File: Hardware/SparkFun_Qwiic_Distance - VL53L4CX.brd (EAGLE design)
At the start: 25.4 x 25.4 mm, 25 parts, among them J2 QWIIC_RIGHT_ANGLE, J4 QWIIC_RIGHT_ANGLE, U1 VL53L4X

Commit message: Adds silk to the product
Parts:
- added LOGO2: SFE_LOGO_NAME.1_INCH, SparkFun-Aesthetics:SFE_LOGO_NAME_.1
- added LOGO3: QWIIC_LOGO_4MM, SparkFun-Aesthetics:QWIIC_4MM
- added U$1: (no value), distanceSensor:##INT##7
- added U$10: (no value), distanceSensor:#LED#54
- added U$11: (no value), distanceSensor:#INT#55
- added U$12: (no value), distanceBot:##INT##7
- added U$13: (no value), distanceBot:##SHUT##6
- added U$14: (no value), distanceBot:#3V3#1
- added U$15: (no value), distanceBot:#GND#0
- added U$16: (no value), distanceBot:#SCL#4
- added U$17: (no value), distanceBot:#SDA#5
- added U$18, U$8: (no value), distanceSensor:DISTANCE_SENSOR8
- added U$19, U$9: (no value), distanceSensor:VL53L4CX9
- added U$2: (no value), distanceSensor:##SHUT##6
- added U$20: (no value), distanceSensor:DEF_ADDR#54
- added U$21: (no value), distanceSensor:0X2955
- added U$22: (no value), SparkFun-Aesthetics:SFE_LOGO_FLAME_.1
- added U$3: (no value), distanceSensor:#3V3#1
- added U$4: (no value), distanceSensor:#GND#0
- added U$5: (no value), distanceSensor:#I2C#56
- added U$6: (no value), distanceSensor:#SCL#4
- added U$7: (no value), distanceSensor:#SDA#5
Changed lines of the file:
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@@
 <layer number="45" name="Holes" color="7" fill="1" visible="yes" active="yes"/>
 <layer number="46" name="Milling" color="3" fill="1" visible="no" active="yes"/>
-<layer number="47" name="Measures" color="7" fill="1" visible="yes" active="yes"/>
+<layer number="47" name="Measures" color="7" fill="1" visible="no" active="yes"/>
 <layer number="48" name="Document" color="7" fill="1" visible="no" active="yes"/>
 <layer number="49" name="Reference" color="13" fill="1" visible="yes" active="yes"/>
@@
 <attribute name="VALUE" x="2.032" y="5.842" size="0.6096" layer="28" font="vector" ratio="20" rot="MR0" align="top-center"/>
 </element>
+<element name="U$1" library="distanceSensor" package="##INT##7" value="" x="16.51" y="3.683" smashed="yes" rot="R270"/>
+<element name="U$2" library="distanceSensor" package="##SHUT##6" value="" x="19.05" y="4.445" smashed="yes" rot="R270"/>
+<element name="U$3" library="distanceSensor" package="#3V3#1" value="" x="8.89" y="3.937" smashed="yes" rot="R270"/>
+<element name="U$4" library="distanceSensor" package="#GND#0" value="" x="6.35" y="4.064" smashed="yes" rot="R270"/>
+<element name="U$5" library="distanceSensor" package="#I2C#56" value="" x="12.573" y="19.431" smashed="yes" rot="MR0"/>
+<element name="U$6" library="distanceSensor" package="#SCL#4" value="" x="13.97" y="3.81" smashed="yes" rot="R270"/>
+<element name="U$7" library="distanceSensor" package="#SDA#5" value="" x="11.43" y="3.937" smashed="yes" rot="R270"/>
+<element name="U$8" library="distanceSensor" package="DISTANCE_SENSOR8" value="" x="12.7" y="21.717" smashed="yes"/>
+<element name="U$9" library="distanceSensor" package="VL53L4CX9" value="" x="12.7" y="20.32" smashed="yes"/>
+<element name="U$10" library="distanceSensor" package="#LED#54" value="" x="4.572" y="6.985" smashed="yes" rot="MR0"/>
+<element name="U$11" library="distanceSensor" package="#INT#55" value="" x="10.16" y="12.7" smashed="yes" rot="MR0"/>
+<element name="U$12" library="distanceBot" package="##INT##7" value="" x="16.51" y="3.683" smashed="yes" rot="MR90"/>
+<element name="U$13" library="distanceBot" package="##SHUT##6" value="" x="19.05" y="4.445" smashed="yes" rot="MR90"/>
+<element name="U$14" library="distanceBot" package="#3V3#1" value="" x="8.89" y="3.937" smashed="yes" rot="MR90"/>
+<element name="U$15" library="distanceBot" package="#GND#0" value="" x="6.35" y="4.064" smashed="yes" rot="MR90"/>
+<element name="U$16" library="distanceBot" package="#SCL#4" value="" x="13.97" y="3.81" smashed="yes" rot="MR90"/>
+<element name="U$17" library="distanceBot" package="#SDA#5" value="" x="11.43" y="3.937" smashed="yes" rot="MR90"/>
+<element name="U$18" library="distanceSensor" package="DISTANCE_SENSOR8" value="" x="12.446" y="24.003" smashed="yes" rot="MR0"/>
+<element name="U$19" library="distanceSensor" package="VL53L4CX9" value="" x="12.7" y="22.606" smashed="yes" rot="MR0"/>
+<element name="U$20" library="distanceSensor" package="DEF_ADDR#54" value="" x="14.224" y="20.955" smashed="yes" rot="MR0"/>
+<element name="U$21" library="distanceSensor" package="0X2955" value="" x="9.652" y="20.955" smashed="yes" rot="MR0"/>
+<element name="LOGO2" library="SparkFun-Aesthetics" package="SFE_LOGO_NAME_.1" value="SFE_LOGO_NAME.1_INCH" x="12.7" y="23.368" smashed="yes"/>
+<element name="LOGO3" library="SparkFun-Aesthetics" package="QWIIC_4MM" value="QWIIC_LOGO_4MM" x="2.286" y="17.272" smashed="yes"/>
+<element name="U$22" library="SparkFun-Aesthetics" package="SFE_LOGO_FLAME_.1" value="" x="5.588" y="22.479" smashed="yes" rot="MR0"/>
 </elements>
 <signals>

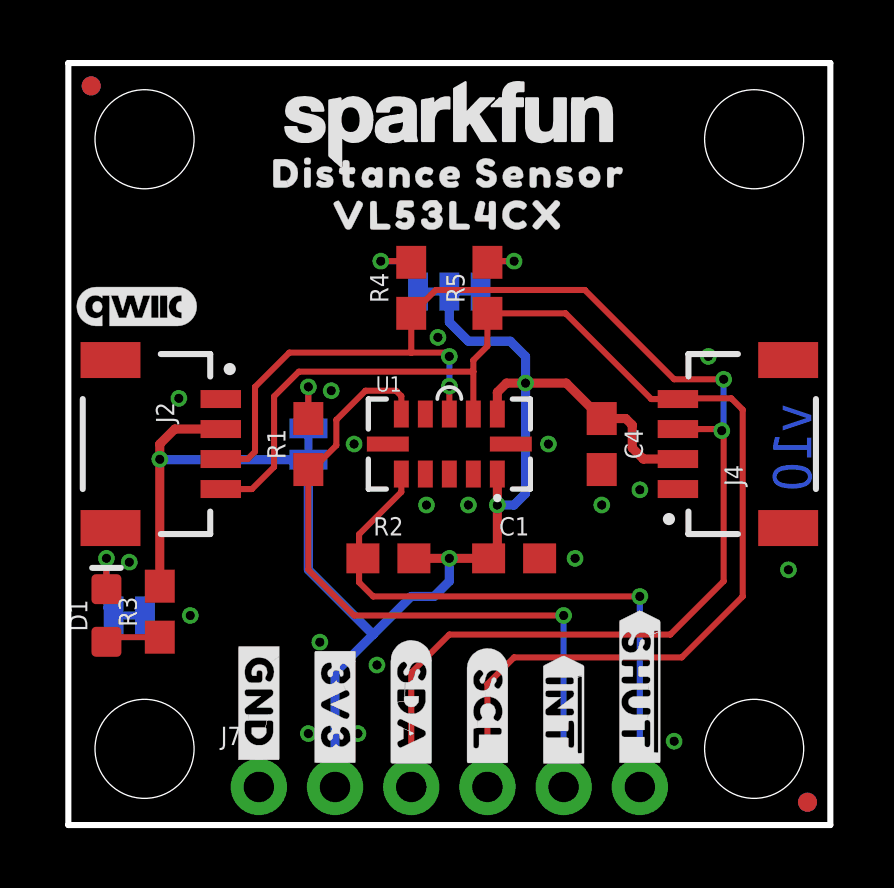
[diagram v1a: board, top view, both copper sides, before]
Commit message: Replaces INT silk with OUTPUT style flag, adds revised by to attribution in board
* 3.3V traces bumped to 16mils
* Moves some silk to keep them from touching
* Adds PWR silk
* Adjusts some overlapping part labels
* Corrects distance sensor name in library
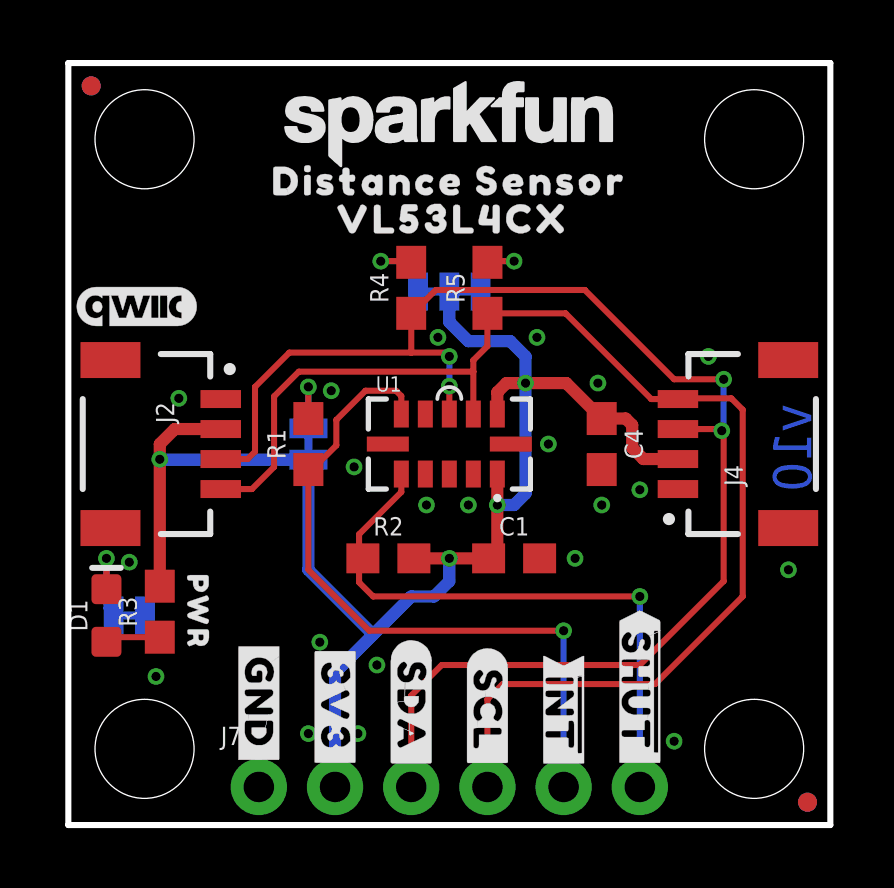
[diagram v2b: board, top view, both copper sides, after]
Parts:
- added U$23: (no value), distanceSensor:PWR55
- U1: value VL53L4X -> VL53L4CX; device DISTANCE:VL53L4X -> DISTANCE:VL53L4CX
- moved U$8 0.25 mm to (12.7, 21.5)
- moved U$9 0.18 mm to (12.8, 20.2)
- renumbered JP10 to PWR
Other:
- board text added: "Nate Seidle"
- board text added: "Revised By:"
